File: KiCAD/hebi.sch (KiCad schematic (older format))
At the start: 15 parts

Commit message: Finished most of the schematic (except power selection).
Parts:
- removed C? (x2): 22pF, ~, symbol C
- removed C?: C, ~, symbol C
- removed D?: LED, ~, symbol LED
- removed K?: SERVO0, ~, symbol CONN_3
- removed K?: SERVO1, ~, symbol CONN_3
- removed K?: SERVO2, ~, symbol CONN_3
- removed P?: nRF2401L, ~, symbol CONN_4X2
- removed P?: SERIAL, ~, symbol CONN_4
- removed P?: EXPANSION, ~, symbol CONN_4X2
- removed R?: 10K, ~, symbol R
- removed R?: 680, ~, symbol R
- removed SW?: SW_PUSH, ~, symbol SW_PUSH
- removed U?: ATMEGA328P, symbol ATMEGA168
- removed X?: 16Mhz, ~, symbol CRYSTAL
- added C1, C13, C14, C16, C17, C19, C20, C21, C23, C24, C8, C9: 100nF, ~, symbol C
- added C10: 4.7uF X7R 0805, ~, symbol CP1
- added C11: 22uF, ~, symbol C
- added C12: 1uF X7R 0805, ~, symbol CP1
- added C15, C18: 2.2uF, ~, symbol C
- added C2, C3: 20pF, ~, symbol C
- added C22: 22uF, ~, symbol CP1
- added C25: 1uF, ~, symbol C
- added C26: 10uF, ~, symbol C
- added C4: 10nF, ~, symbol C
- added C5: 4.7uF, ~, symbol C
- added C6, C7: 1uF, ~, symbol CP1
- added CR1, CR2: CG0603MLC-05LE, symbol ESD
- added D1: GREEN, ~, symbol LED
- added D2: ORANGE, ~, symbol LED
- added D3: RED, ~, symbol LED
- added D4: BLUE, ~, symbol LED
- added F1: MF-MSMF050-2, symbol FUSE-MINI
- added JP1: JP_5, symbol JP_5
- added JP2, JP3, JP4, JP5: JUMPER-2, symbol JUMPER-2
- added K1, K2, K3, K4, K5: CONN_3, ~, symbol CONN_3
- added L1: fcm 0603, ~, symbol INDUCTOR_SMALL
- added P1, P2, P3, P4: CONN_4, ~, symbol CONN_4
- added P5, P6: CONN_2, ~, symbol CONN_2
- added Q1: FDN340P, ~, symbol MOS_P_DIODE
- added Q10, Q11, Q2, Q3, Q4, Q5, Q6, Q7, Q8: MOS_N_DIODE, ~, symbol MOS_N_DIODE
- added Q9: MOS_N, ~, symbol MOS_N
- added R1, R14, R3, R36, R37: 4.7K, ~, symbol R
- added R10, R6: 510, ~, symbol R
- added R11, R31: R, ~, symbol R
- added R12, R13: 22R, ~, symbol R
- added R15, R16, R17, R18, R19, R20, R21, R22, R23, R24, R25, R26, R27, R28, R29, R30, R32, R33, R34, R35: 10K, ~, symbol R
- added R2: 100K, ~, symbol R
- added R4: 220K, ~, symbol R
- added R5: 47, ~, symbol R
- added R7, R8, R9: 680, ~, symbol R
- added SW1, SW2, SW3: SW_PUSH, ~, symbol SW_PUSH
- added U1: L3GD20, symbol L3GD20
- added U2: LSM303DLHC, symbol LSM303DLHC
- added U3: MCP1825S, ~, symbol MCP1825S
- added U4: STM32F407VG, TQFP100, symbol STM32F407VG
- added U5: XBEE, symbol XBEE
- added U6: 74AHC2G126, ~, symbol 74AHC2G126
- added USB1: USBCONN, symbol USBCONN
- added X1: 8MHz, ~, symbol CRYSTAL
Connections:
- net labels added: ACC_INT_1, ACC_INT_2, ADC1, ADC2, ADC3, BOOT0, BOOT1, D+, D-, DATA_DYN, DIR_PORT_DYN, GYRO_INT_1, GYRO_INT_2, I2C_PCB_SCL, I2C_PCB_SDA, I2C_SCL_PWR_3V, I2C_SCL_PWR_5V, I2C_SDA_PWR_3V, I2C_SDA_PWR_5V, LED1, LED2, LED3, LED4, PUSH_SW, RX1, RX2, RX3, RX4, RX_DYN, SERVO1_3V, SERVO1_5V, SERVO2_3V, SERVO2_5V, SERVO3_3V, SERVO3_5V, SERVO_PWR, SPI1_MISO, SPI1_MOSI, SPI1_NSS, SPI1_SCK, SWCLK, SWDIO, TX1, TX1_3V, TX2, TX2_3V, TX3, TX3_3V, TX4, TX4_3V, TX_DYN, T_SWO, VBUS, VCC, VIN, VUSB, Vin, XBEE_RESET, XBEE_RX, XBEE_SLEEP, XBEE_TX
- net labels removed: 3.3V, AINSRV0, AINSRV1, AINSRV2, EXTRA0, EXTRA1, EXTRA2, EXTRA3, EXTRA4, MISO, MOSI, RF24CE, RF24CSN, RX, SCK, SCL, SDA, SERVO0, SERVO1, SERVO2, TX
- wire segments 75 -> 526
- no-connect marks 1 -> 58
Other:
- note added: "'0' > from flash\n'1' > DFU Mode"
- note added: "ADC connector"
- note added: "Analog power supply"
- note added: "BOOT configuration \n(for enabling the bootloader)"
- note added: "Connector for the power suppy module"
- note added: "DYNAMIXEL servo control"
- note added: "Inertial Measurement Unit (IMU)"
- note added: "It might be useful to \nmake VSSA to go to\na analog ground plane"
- note added: "LDO Power Regulator\nIn: 5-6V Out: 3V"
- note added: "LED indicators"
- note added: "NOTE: VBAT is the RTC backup \npower supply, and must lie \nbetween 1.65V and 3.6V\n"
- note added: "Power Flags"
- note added: "Power supply filtering"
- note added: "RESET button"
- note added: "SERVO headers"
- note added: "STM32F4 Microcontroller"
- note added: "SWD (Serial wire debugging) connector\n"
- note added: "Serial ports to other modules"
- note added: "Since this needs 9.6V to work \nI'm currently thinking of breaking\nout the 3 control pins ( Rx, Tx, Dir)\nto connect them to an expansion \nmodule."
- note added: "TODO: Assign interrupts to pins"
- note added: "USB Port"
- note added: "USB Power Switch"
- note added: "USER button"
- note added: "xBee connector"

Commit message: Added or-ing circuit
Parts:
- removed Q1: FDN340P, ~, symbol MOS_P_DIODE
- removed R15: 10K, ~, symbol R
- added D? (x2): D_SCHOTTKY, ~, symbol D_SCHOTTKY
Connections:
- wire segments 526 -> 527
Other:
- note added: "or-ing power supplies circuit"
- note removed: "USB Power Switch"
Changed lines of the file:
@@
-EESchema Schematic File Version 2  date Thu 30 Jan 2014 12:43:37 CET
+EESchema Schematic File Version 2  date Fri 31 Jan 2014 13:14:15 CET
 LIBS:power
 LIBS:device
@@
 Sheet 1 1
 Title "HEBI - Electronic Board for Modular Robots (STM32F4 flavour)"
-Date "30 jan 2014"
+Date "31 jan 2014"
 Rev "0.1.0"
 Comp "David Estévez Fernández"
@@
 D-
 NoConn ~ 4150 6500
-Text Label 12800 10600 0    60   ~ 0
+Text Label 12900 10900 0    60   ~ 0
 VUSB
 $Comp
 L +5V #PWR026
 U 1 1 52EA5685
-P 14000 10600
-F 0 "#PWR026" H 14000 10690 20  0001 C CNN
-F 1 "+5V" H 14000 10690 30  0000 C CNN
-F 2 "" H 14000 10600 60  0000 C CNN
-F 3 "" H 14000 10600 60  0000 C CNN
-	1    14000 10600
+P 14000 10700
+F 0 "#PWR026" H 14000 10790 20  0001 C CNN
+F 1 "+5V" H 14000 10790 30  0000 C CNN
+F 2 "" H 14000 10700 60  0000 C CNN
+F 3 "" H 14000 10700 60  0000 C CNN
+	1    14000 10700
 	1    0    0    -1
 $EndComp
-$Comp
-L R R15
-U 1 1 52EA568B
-P 13150 10900
-F 0 "R15" V 13230 10900 40  0000 C CNN
-F 1 "10K" V 13157 10901 40  0000 C CNN
-F 2 "~" V 13080 10900 30  0000 C CNN
-F 3 "~" H 13150 10900 30  0000 C CNN
-	1    13150 10900
-	-1   0    0    1
-$EndComp
-$Comp
-L GND #PWR027
-U 1 1 52EA5691
-P 13150 11200
-F 0 "#PWR027" H 13150 11200 30  0001 C CNN
-F 1 "GND" H 13150 11130 30  0001 C CNN
-F 2 "" H 13150 11200 60  0000 C CNN
-F 3 "" H 13150 11200 60  0000 C CNN
-	1    13150 11200
-	1    0    0    -1
-$EndComp
-$Comp
-L MOS_P_DIODE Q1
-U 1 1 52EA5697
-P 13550 10500
-F 0 "Q1" V 13500 10750 60  0000 R CNN
-F 1 "FDN340P" V 13850 10700 60  0000 R CNN
-F 2 "~" H 13550 10500 60  0000 C CNN
-F 3 "~" H 13550 10500 60  0000 C CNN
-	1    13550 10500
-	0    -1   1    0
-$EndComp
-Text Label 12800 10300 0    60   ~ 0
+Text Label 12900 10500 0    60   ~ 0
 Vin
-Text Notes 13300 11350 0    60   ~ 0
-USB Power Switch
+Text Notes 12800 11250 0    60   ~ 0
+or-ing power supplies circuit
 $Comp
 L XBEE U5
@@
 	4150 6700 3300 6700
 Wire Wire Line
-	12800 10300 13650 10300
-Wire Wire Line
-	13750 10600 14000 10600
-Wire Wire Line
-	12800 10600 13150 10600
-Wire Wire Line
-	13150 10600 13350 10600
-Wire Wire Line
-	13150 11200 13150 11150
-Wire Wire Line
-	13150 10650 13150 10600
-Connection ~ 13150 10600
+	13600 10700 14000 10700
 Wire Notes Line
-	12650 10150 14150 10150
+	12650 10150 14400 10150
 Wire Notes Line
-	14150 10150 14150 11400
+	14400 10150 14400 11400
 Wire Notes Line
-	14150 11400 12650 11400
+	14400 11400 12650 11400
 Wire Notes Line
 	12650 11400 12650 10150
@@
 	7650 13400 7650 13250
 $Comp
-L PWR_FLAG #FLG?
+L PWR_FLAG #FLG079
 U 1 1 52EAABAC
 P 7400 10400
-F 0 "#FLG?" H 7400 10495 30  0001 C CNN
+F 0 "#FLG079" H 7400 10495 30  0001 C CNN
 F 1 "PWR_FLAG" H 7400 10580 30  0000 C CNN
 F 2 "" H 7400 10400 60  0000 C CNN
@@
 	7400 10400 7400 10650
 Text Label 7400 10650 1    60   ~ 0
-VUSB
+VBUS
+$Comp
+L D_SCHOTTKY D?
+U 1 1 52EB9345
+P 13400 10500
+F 0 "D?" V 13310 10450 35  0000 C CNN
+F 1 "D_SCHOTTKY" V 13500 10425 30  0000 C CNN
+F 2 "~" H 13400 10500 60  0000 C CNN
+F 3 "~" H 13400 10500 60  0000 C CNN
+	1    13400 10500
+	1    0    0    -1
+$EndComp
+$Comp
+L D_SCHOTTKY D?
+U 1 1 52EB9352
+P 13400 10900
+F 0 "D?" V 13310 10850 35  0000 C CNN
+F 1 "D_SCHOTTKY" V 13500 10825 30  0000 C CNN
+F 2 "~" H 13400 10900 60  0000 C CNN
+F 3 "~" H 13400 10900 60  0000 C CNN
+	1    13400 10900
+	1    0    0    -1
+$EndComp
+Wire Wire Line
+	13550 10500 13600 10500
+Wire Wire Line
+	13600 10500 13600 10700
+Wire Wire Line
+	13600 10700 13600 10900
+Wire Wire Line
+	13600 10900 13550 10900
+Connection ~ 13600 10700
+Wire Wire Line
+	13250 10500 12900 10500
+Wire Wire Line
+	12900 10900 13250 10900
 $EndSCHEMATC

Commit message: ERC checked. Generated Netlist.
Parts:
- gave numbers to parts that had none: 2
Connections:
- wire segments 527 -> 413

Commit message: Modified some schematic values.
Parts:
- C11: value 22uF -> 220nF
- C2, C3: value 20pF -> 24pF
- C26: value 10uF -> 1uF
- R11: value R -> 510
- R31: value R -> 4.7K
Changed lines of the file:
@@
-EESchema Schematic File Version 2  date Fri 31 Jan 2014 13:16:39 CET
+EESchema Schematic File Version 2  date Fri 07 Feb 2014 13:18:56 CET
 LIBS:power
 LIBS:device
@@
 Sheet 1 1
 Title "HEBI - Electronic Board for Modular Robots (STM32F4 flavour)"
-Date "31 jan 2014"
+Date "7 feb 2014"
 Rev "0.1.0"
 Comp "David Estévez Fernández"
@@
 P 9350 13900
 F 0 "R11" V 9430 13900 40  0000 C CNN
-F 1 "R" V 9357 13901 40  0000 C CNN
+F 1 "510" V 9357 13901 40  0000 C CNN
 F 2 "~" V 9280 13900 30  0000 C CNN
 F 3 "~" H 9350 13900 30  0000 C CNN
@@
 P 2950 4100
 F 0 "C2" V 2900 4200 40  0000 L CNN
-F 1 "20pF" V 3000 3900 40  0000 L CNN
+F 1 "24pF" V 3000 3900 40  0000 L CNN
 F 2 "~" H 2988 3950 30  0000 C CNN
 F 3 "~" H 2950 4100 60  0000 C CNN
@@
 P 2950 4700
 F 0 "C3" V 2900 4800 40  0000 L CNN
-F 1 "20pF" V 3000 4500 40  0000 L CNN
+F 1 "24pF" V 3000 4500 40  0000 L CNN
 F 2 "~" H 2988 4550 30  0000 C CNN
 F 3 "~" H 2950 4700 60  0000 C CNN
@@
 P 20600 5750
 F 0 "C26" H 20600 5850 40  0000 L CNN
-F 1 "10uF" H 20606 5665 40  0000 L CNN
+F 1 "1uF" H 20606 5665 40  0000 L CNN
 F 2 "~" H 20638 5600 30  0000 C CNN
 F 3 "~" H 20600 5750 60  0000 C CNN
@@
 P 19200 2150
 F 0 "R31" V 19280 2150 40  0000 C CNN
-F 1 "R" V 19207 2151 40  0000 C CNN
+F 1 "4.7K" V 19207 2151 40  0000 C CNN
 F 2 "~" V 19130 2150 30  0000 C CNN
 F 3 "~" H 19200 2150 30  0000 C CNN
@@
 P 7950 13750
 F 0 "C11" H 7950 13850 40  0000 L CNN
-F 1 "22uF" H 7956 13665 40  0000 L CNN
+F 1 "220nF" H 7956 13665 40  0000 L CNN
 F 2 "~" H 7988 13600 30  0000 C CNN
 F 3 "~" H 7950 13750 60  0000 C CNN
@@
 U 1 1 52EB9345
 P 13400 10500
-F 0 "D5" V 13310 10450 35  0000 C CNN
-F 1 "D_SCHOTTKY" V 13500 10425 30  0000 C CNN
+F 0 "D5" H 13300 10550 35  0000 C CNN
+F 1 "D_SCHOTTKY" H 13400 10400 30  0000 C CNN
 F 2 "~" H 13400 10500 60  0000 C CNN
 F 3 "~" H 13400 10500 60  0000 C CNN
@@
 U 1 1 52EB9352
 P 13400 10900
-F 0 "D6" V 13310 10850 35  0000 C CNN
-F 1 "D_SCHOTTKY" V 13500 10825 30  0000 C CNN
+F 0 "D6" H 13300 10950 35  0000 C CNN
+F 1 "D_SCHOTTKY" H 13400 10800 30  0000 C CNN
 F 2 "~" H 13400 10900 60  0000 C CNN
 F 3 "~" H 13400 10900 60  0000 C CNN

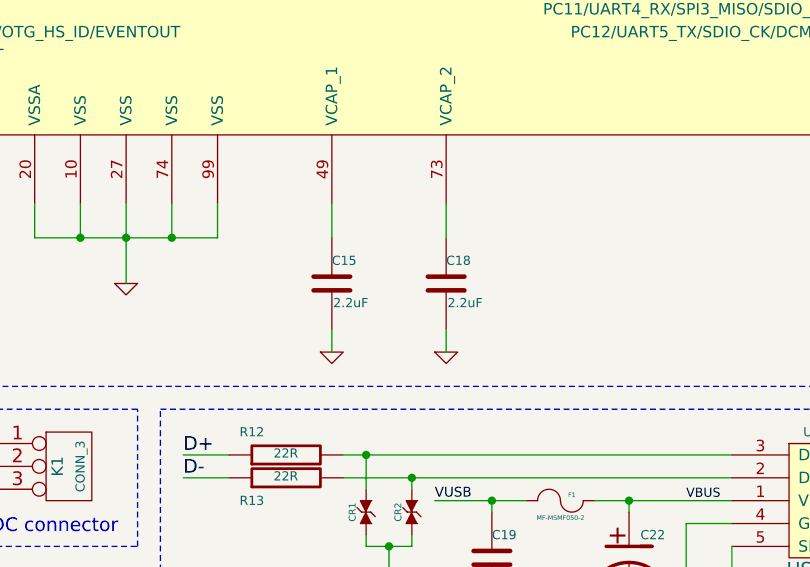
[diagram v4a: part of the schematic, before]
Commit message: Assigned some footprints to netlist.
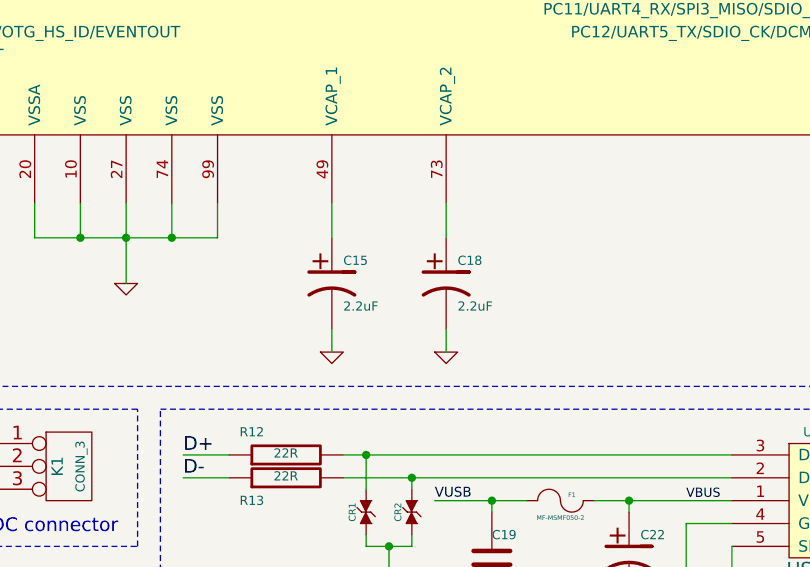
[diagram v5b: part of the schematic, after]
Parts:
- removed C15, C18: 2.2uF, ~, symbol C
- added C15, C18: 2.2uF, ~, symbol CP1
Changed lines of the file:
@@
-EESchema Schematic File Version 2  date Fri 07 Feb 2014 13:18:56 CET
+EESchema Schematic File Version 2  date Mon 10 Feb 2014 12:02:56 CET
 LIBS:power
 LIBS:device
@@
 Sheet 1 1
 Title "HEBI - Electronic Board for Modular Robots (STM32F4 flavour)"
-Date "7 feb 2014"
+Date "10 feb 2014"
 Rev "0.1.0"
 Comp "David Estévez Fernández"
@@
 SWCLK
 $Comp
-L C C15
-U 1 1 52EA557D
-P 10050 9600
-F 0 "C15" H 10050 9700 40  0000 L CNN
-F 1 "2.2uF" H 10056 9515 40  0000 L CNN
-F 2 "~" H 10088 9450 30  0000 C CNN
-F 3 "~" H 10050 9600 60  0000 C CNN
-	1    10050 9600
-	1    0    0    -1
-$EndComp
-$Comp
 L SW_PUSH SW3
 U 1 1 52EA5583
@@
 BOOT0
 $Comp
-L C C18
-U 1 1 52EA558A
-P 10550 9600
-F 0 "C18" H 10550 9700 40  0000 L CNN
-F 1 "2.2uF" H 10556 9515 40  0000 L CNN
-F 2 "~" H 10588 9450 30  0000 C CNN
-F 3 "~" H 10550 9600 60  0000 C CNN
-	1    10550 9600
-	1    0    0    -1
-$EndComp
-$Comp
 L GND #PWR012
 U 1 1 52EA5590
@@
 Wire Wire Line
 	12900 10900 13250 10900
+$Comp
+L CP1 C15
+U 1 1 52F8B1B8
+P 10050 9600
+F 0 "C15" H 10100 9700 40  0000 L CNN
+F 1 "2.2uF" H 10100 9500 40  0000 L CNN
+F 2 "~" H 10050 9600 60  0000 C CNN
+F 3 "~" H 10050 9600 60  0000 C CNN
+	1    10050 9600
+	1    0    0    -1
+$EndComp
+$Comp
+L CP1 C18
+U 1 1 52F8B1E2
+P 10550 9600
+F 0 "C18" H 10600 9700 40  0000 L CNN
+F 1 "2.2uF" H 10600 9500 40  0000 L CNN
+F 2 "~" H 10550 9600 60  0000 C CNN
+F 3 "~" H 10550 9600 60  0000 C CNN
+	1    10550 9600
+	1    0    0    -1
+$EndComp
 $EndSCHEMATC

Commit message: Added new magnetic compass.
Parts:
- removed C5: 4.7uF, ~, symbol C
- removed U2: LSM303DLHC, symbol LSM303DLHC
- added C5: 4.7uF, ~, symbol CP1
- added U?: HMC5883L, ~, symbol HMC5883L
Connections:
- net labels added: COMPASS_INT, COMPASS_iNT
- net labels removed: ACC_INT_1, ACC_INT_2
- wire segments 413 -> 524
- no-connect marks 58 -> 62
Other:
- note removed: "TODO: Assign interrupts to pins"
- moved on the sheet: C11, R36, R37

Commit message: Solved IMU issue on schematic, changed annotation.
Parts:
- removed R1, R3: 4.7K, ~, symbol R
- removed U1: L3GD20, symbol L3GD20
- removed U?: HMC5883L, ~, symbol HMC5883L
- added C1, C3: 0.1uF, ~, symbol C
- added C2: 10nF, ~, symbol C
- added JP1: JUMPER3, ~, symbol JUMPER3
- added U1: MPU-6050, ~, symbol MPU-6050
- added U2: HMC5883L, ~, symbol HMC5883L
- C4: value 10nF -> 2.2nF
- renumbered C7 to C10, C8 to C11, C9 to C12, C10 to C13, C11 to C14, C12 to C15, C13 to C16, C14 to C17, C15 to C18, C16 to C19, C17 to C20, C18 to C21, C19 to C22, C20 to C23, C21 to C24, C22 to C25, C23 to C26, C24 to C27, C25 to C28, C26 to C29, C1 to C5, C2 to C6, C3 to C7, C5 to C8, C6 to C9, JP1 to JP2, JP2 to JP3, JP3 to JP4, JP4 to JP5, JP5 to JP6, Q2 to Q1, Q11 to Q10, Q3 to Q2, Q4 to Q3, Q5 to Q4, Q6 to Q5, Q7 to Q6, Q8 to Q7, Q9 to Q8, Q10 to Q9, R2 to R1, R16 to R15, R17 to R16, R18 to R17, R19 to R18, R20 to R19, R4 to R2, R21 to R20, R22 to R21, R23 to R22, R24 to R23, R25 to R24, R26 to R25, R27 to R26, R28 to R27, R29 to R28, R30 to R29, R5 to R3, R31 to R30, R32 to R31, R33 to R32, R34 to R33, R35 to R34, R36 to R4, R6 to R5, R7 to R6, R8 to R7, R9 to R8, R37 to R9
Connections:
- net labels added: ACCEL_INT
- net labels removed: GYRO_INT_1, GYRO_INT_2
- wire segments 524 -> 405
- no-connect marks 62 -> 76
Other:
- note added: "C1 - Ceramic, X7R, 0.1uF, tol 10%, 4V\nC2 - Ceramic, X7R, 10nF, tol 10%, 4V\nC3 - Ceramic, X7R, 0.1uF, tol 10%, 2V\nC4 - Ceramic, X7R, 2.2, tol 10%, 50V"
